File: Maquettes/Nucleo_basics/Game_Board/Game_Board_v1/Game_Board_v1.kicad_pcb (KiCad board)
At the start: 2 copper layers, 150 x 100 mm, 42 parts, among them CON1 MikroE-nRF-S-module, J1 TFT-RB1.8, J2 JOYSTICK, J3 AnalogIn, J4 AnalogChoice, SW1 SW_Push, SW2 SW_Push, SW3 SW_Push, SW4 SW_Push, U1 NUCLEO-L432KC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

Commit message: Update GameBoard
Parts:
- removed R14, R15: 220, Resistor_THT:R_Axial_DIN0207_L6.3mm_D2.5mm_P10.16mm_Horizontal
- removed R16, R17, R18: 1k, Resistor_THT:R_Axial_DIN0207_L6.3mm_D2.5mm_P10.16mm_Horizontal
- added J5: Conn_01x02, TerminalBlock_Phoenix:TerminalBlock_Phoenix_PT-1,5-2-5.0-H_1x02_P5.00mm_Horizontal, F.Cu at (179.5, 154.5)
- added J6: Conn_01x04, Connector_PinHeader_2.54mm:PinHeader_1x04_P2.54mm_Horizontal, F.Cu at (259.1, 151.0)
- R11, R12, R13: value 220 -> 1k
- R3: value 220 -> 1.2k
- R4: value 220 -> 12k
- R5: value 1.2k -> 12k
- R8, R9: value 12k -> 220
- RV1: value R_POT_TRIM -> R_10k
- SW1, SW2, SW3, SW4: footprint Resistor_THT:R_Axial_DIN0207_L6.3mm_D2.5mm_P5.08mm_Vertical -> LEnsE_devices:Switch
- moved D1 135.8 mm to (147.9, 159.5)
- moved D2 132.6 mm to (148.0, 156.0)
- moved C5 132.4 mm to (154.0, 148.0), turned to 180 degrees
- moved R6 119.8 mm to (138.9, 146.6)
- moved R3 100.7 mm to (145.4, 152.1), turned to 0 degrees
- moved R10 95.2 mm to (239.3, 71.0), turned to 0 degrees
- moved R9 90.0 mm to (239.3, 75.0), turned to 0 degrees
- moved R8 88.8 mm to (261.8, 70.9), turned to 0 degrees
- moved R12 84.7 mm to (205.8, 149.0)
- moved R7 84.6 mm to (261.8, 75.0), turned to 0 degrees
- moved R2 78.1 mm to (259.3, 83.5), turned to 0 degrees
- moved R1 75.2 mm to (263.8, 89.0), turned to 0 degrees
- moved R11 73.8 mm to (205.8, 145.5), turned to 0 degrees
- moved U2 53.6 mm to (140.2, 84.1), turned to 90 degrees
- moved R5 52.8 mm to (240.5, 108.5), turned to -90 degrees
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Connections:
- C1 pad 1: SW1 -> 3.3V
- C1 pad 2: GND -> SW1
- C2 pad 1: SW2 -> 3.3V
- C2 pad 2: GND -> SW2
- C3 pad 1: SW_JOY_OUT -> 3.3V
- C3 pad 2: GND -> SW3
- C4 pad 1: SW3 -> 3.3V
- C4 pad 2: GND -> SW4
- C5 pad 1: SW4 -> 3.3V
- C5 pad 2: GND -> JOYSW
- D1 pad 2: Net-(D1-A) -> AN_IN
- D2 pad 1: Net-(D1-A) -> AN_IN
- D5 pad 1: unconnected-(D5-K-Pad1) -> Net-(D5-K)
- R1 pad 1: Net-(R1-Pad1) -> SW1
- R10 pad 1: Net-(R10-Pad1) -> Net-(D6-K)
- R10 pad 2: SW3 -> GND
- R11 pad 1: Net-(R11-Pad1) -> 3.3V
- R11 pad 2: SW4 -> SCL
- R12 pad 1: Net-(D3-K) -> 3.3V
- R12 pad 2: GND -> SDA
- R13 pad 1: Net-(D4-K) -> 3.3V
- R13 pad 2: GND -> Net-(U3-~{RESET})
- R2 pad 1: Net-(R2-Pad1) -> SW2
- R3 pad 1: Net-(R1-Pad1) -> Net-(J3-Pin_2)
- R3 pad 2: SW1 -> AN_IN
- R4 pad 1: Net-(R2-Pad1) -> SW3
- R4 pad 2: SW2 -> GND
- R5 pad 1: Net-(J3-Pin_2) -> SW4
- R5 pad 2: Net-(D1-A) -> GND
- R7 pad 1: JOYSW -> Net-(D3-K)
- R7 pad 2: SW_JOY_OUT -> GND
- R8 pad 1: Net-(R10-Pad1) -> Net-(D4-K)
- R9 pad 1: Net-(R11-Pad1) -> Net-(D5-K)
- SW1 pad 2: Net-(R1-Pad1) -> SW1
- SW2 pad 2: Net-(R2-Pad1) -> SW2
- SW3 pad 2: Net-(R10-Pad1) -> SW3
- SW4 pad 2: Net-(R11-Pad1) -> SW4
- U1 pad CN3_5: SW_JOY_OUT -> JOYSW
- U1 pad CN3_7: unconnected-(U1A-PB7-PadCN3_7) -> SDA
- U1 pad CN3_8: LCD_DC -> SCL
- U1 pad CN3_9: unconnected-(U1A-PB1-PadCN3_9) -> LCD_DC
- U1 pad CN4_1: unconnected-(U1B-VIN-PadCN4_1) -> Vin
- U1 pad CN4_4: unconnected-(U1B-+5V-PadCN4_4) -> 5V
- U1 pad CN4_7: SCL -> unconnected-(U1B-PA6-PadCN4_7)
- U1 pad CN4_8: SDA -> unconnected-(U1B-PA5-PadCN4_8)
- U2 pad 1: nRF_INT -> (no net)
- U2 pad 10: (no net) -> EX_nRF_INT
- U2 pad 2: EXP_INT -> (no net)
- U2 pad 3: EX_nRF_INT -> (no net)
- U2 pad 8: (no net) -> nRF_INT
- U2 pad 9: (no net) -> EXP_INT
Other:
- outline, holes or cut-outs redrawn

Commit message: Update GameBoard
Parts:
- added J10: nRF_temp1, Connector_PinSocket_2.54mm:PinSocket_1x02_P2.54mm_Vertical, F.Cu at (241.0, 133.5)
- added J11: nRF_temp2, Connector_PinSocket_2.54mm:PinSocket_1x02_P2.54mm_Vertical, F.Cu at (138.2, 71.6)
- added J7: LCD_TEMp, Connector_PinSocket_2.54mm:PinSocket_1x03_P2.54mm_Vertical, F.Cu at (210.6, 134.4)
- added J8: SD_CS_t1, Connector_PinSocket_2.54mm:PinSocket_1x01_P2.54mm_Vertical, F.Cu at (171.0, 130.6)
- added J9: SD_CS_t1, Connector_PinSocket_2.54mm:PinSocket_1x01_P2.54mm_Vertical, F.Cu at (223.3, 134.6)
- R10, R7, R8, R9: value 220 -> 100
- R11, R12, R13: value 1k -> 680
- moved U2 45.2 mm to (183.8, 71.8), turned to 0 degrees
- moved CON1 23.2 mm to (144.2, 69.1)
- moved R9 22.9 mm to (262.2, 73.7)
- moved R10 22.8 mm to (262.1, 70.4)
- moved R4 19.2 mm to (253.5, 93.5), turned to 180 degrees
- moved C3 18.0 mm to (244.4, 83.5), turned to 180 degrees
- moved R5 17.4 mm to (253.5, 97.0), turned to 180 degrees
- moved R7 15.3 mm to (246.6, 73.7)
- moved R8 15.3 mm to (246.6, 70.5)
- moved R13 15.1 mm to (200.0, 76.8), turned to -90 degrees
- moved C4 13.8 mm to (250.5, 89.0), turned to 180 degrees
- moved SW1 13.0 mm to (265.0, 108.5), turned to 0 degrees
- moved SW2 13.0 mm to (277.5, 112.0), turned to 90 degrees
- moved D3 7.60 mm to (218.4, 70.1)
- moved D4 7.24 mm to (213.0, 69.9)
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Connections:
- U1 pad CN3_1: nRF_CS -> nRF_CS_t
- U1 pad CN3_12: LCD_RES -> LCD_RES_t
- U1 pad CN3_13: EX_nRF_INT -> LCD_CS_t
- U1 pad CN3_2: nRF_RS -> nRF_RS_t
- U1 pad CN3_5: JOYSW -> EX_nRF_INT
- U1 pad CN3_6: SD_CS -> SD_CS_t
- U1 pad CN3_9: LCD_DC -> LCD_DC_t
- U1 pad CN4_6: LCD_CS -> AN_OUT
- U1 pad CN4_9: AN_OUT -> JOYSW
- U2 pad 10: EX_nRF_INT -> (no net)
- U2 pad 11: (no net) -> EX_nRF_INT
- U2 pad 12: (no net) -> nRF_INT
- U2 pad 13: (no net) -> EXP_INT
- U2 pad 8: nRF_INT -> (no net)
- U2 pad 9: EXP_INT -> (no net)
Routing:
- net 3.3V: track 0.00 -> 440.7 mm, vias 0 -> 10
- net SDA: track 0.00 -> 151.6 mm, vias 0 -> 2
- net SCL: track 0.00 -> 150.1 mm, vias 0 -> 2
- net SCK: track 0.00 -> 135.5 mm, vias 0 -> 4
- net EX_nRF_INT: track 0.00 -> 132.1 mm
- net MOSI: track 0.00 -> 109.3 mm
- net MISO: track 0.00 -> 108.9 mm, vias 0 -> 4
- net JOYSW: track 0.00 -> 106.3 mm
- net JOYY: track 0.00 -> 87.2 mm
- net JOYX: track 0.00 -> 81.6 mm
- net SW4: track 0.00 -> 76.5 mm
- net SW2: track 0.00 -> 75.2 mm
- net AN_OUT: track 0.00 -> 68.7 mm
- net Net-(D6-K): track 0.00 -> 66.3 mm
- net SW1: track 0.00 -> 63.0 mm
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- added copper zone on B.Cu, net GND
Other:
- outline, holes or cut-outs redrawn
- board text added: "LEnsE 2024 Game Board"

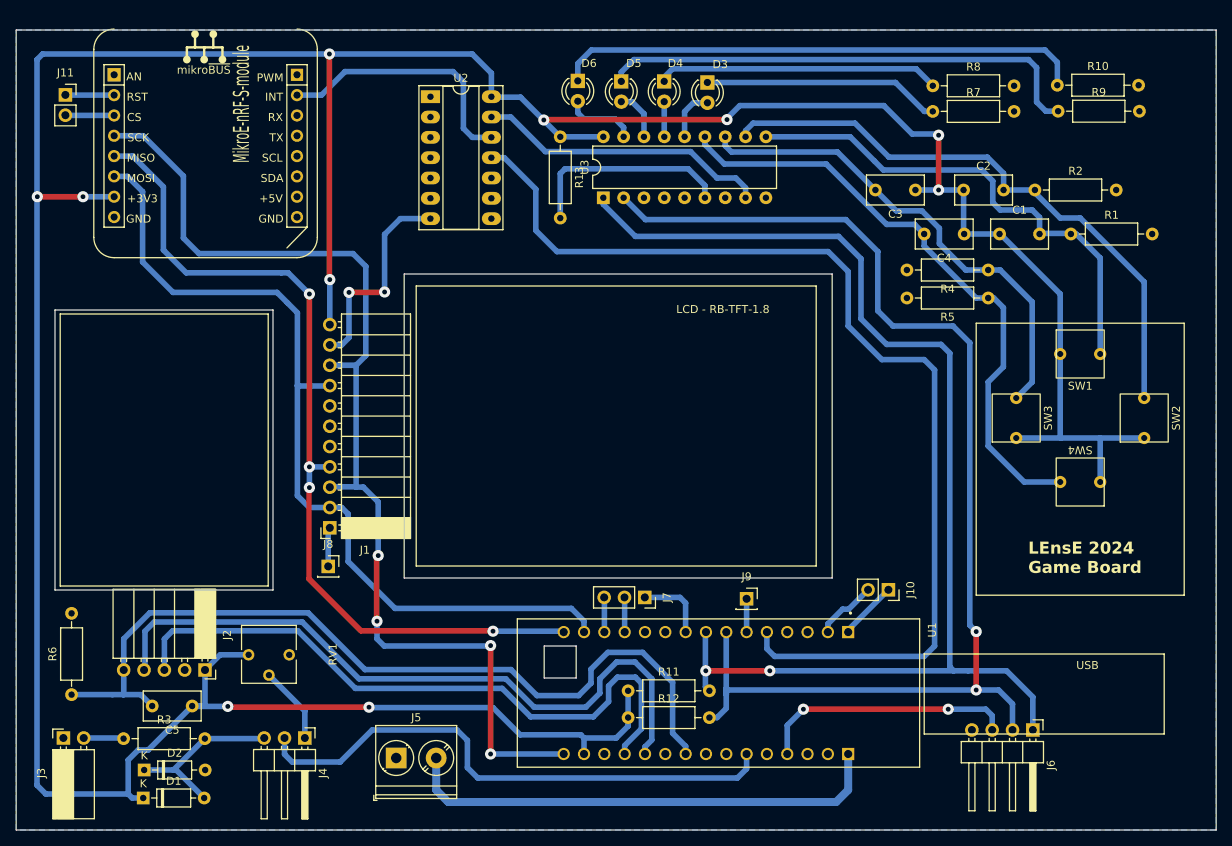
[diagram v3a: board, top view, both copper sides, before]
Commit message: Update Gameboard
Change Joystick connector !!
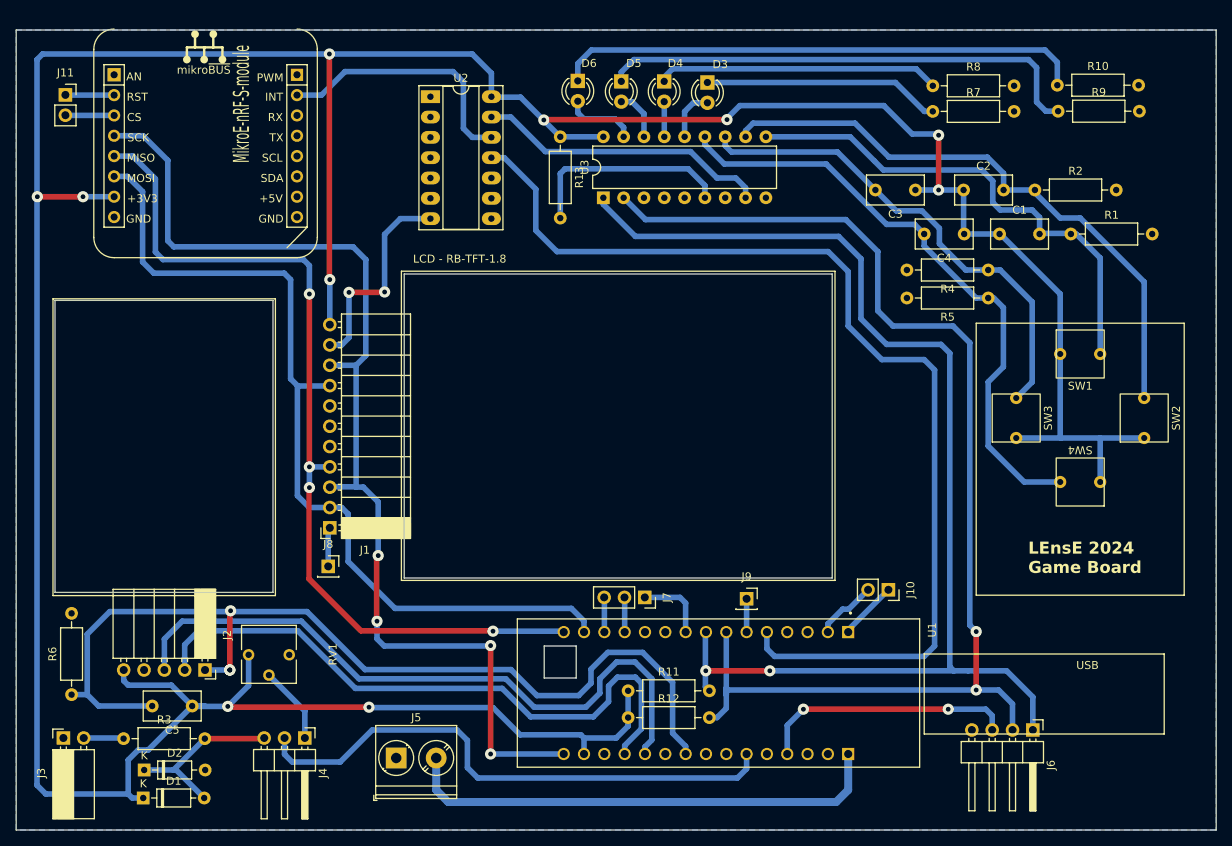
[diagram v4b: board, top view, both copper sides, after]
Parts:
- J6: value Conn_01x04 -> I2C_EXT
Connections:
- J2 pad 1: 3.3V -> JOYSW
- J2 pad 2: GND -> JOYY
- J2 pad 4: JOYY -> GND
- J2 pad 5: JOYSW -> 3.3V
- U1 pad CN4_11: JOYY -> JOYX
- U1 pad CN4_12: JOYX -> JOYY
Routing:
- net JOYSW: track 106.3 -> 121.9 mm, vias 0 -> 3
- net JOYY: track 87.2 -> 78.6 mm
- net 3.3V: track 440.7 -> 448.7 mm
- net MISO: track 108.9 -> 111.8 mm
- net JOYX: track 81.6 -> 84.2 mm
- net MOSI: track 109.3 -> 111.2 mm
- net SCK: track 135.5 -> 137.3 mm
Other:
- outline, holes or cut-outs redrawn

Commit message: Update GameBoard
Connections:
- net nRF_RS renamed nRF_CE
- net nRF_RS_t renamed nRF_CE_t
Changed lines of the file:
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@@
 	(net 11 "unconnected-(CON1-PWM-PadP16)")
 	(net 12 "nRF_INT")
-	(net 13 "nRF_RS")
+	(net 13 "nRF_CE")
 	(net 14 "MISO")
 	(net 15 "MOSI")
@@
 	(net 59 "SD_CS_t")
 	(net 60 "nRF_CS_t")
-	(net 61 "nRF_RS_t")
+	(net 61 "nRF_CE_t")
 	(footprint "Resistor_THT:R_Axial_DIN0207_L6.3mm_D2.5mm_P10.16mm_Horizontal"
 		(layer "F.Cu")
@@
 			(layers "*.Cu" "*.Mask")
 			(remove_unused_layers no)
-			(net 61 "nRF_RS_t")
+			(net 61 "nRF_CE_t")
 			(pinfunction "Pin_2")
 			(pintype "passive")
@@
 			(layers "*.Cu" "*.Mask")
 			(remove_unused_layers no)
-			(net 13 "nRF_RS")
+			(net 13 "nRF_CE")
 			(pinfunction "Pin_1")
 			(pintype "passive")
@@
 			(layers "*.Cu" "*.Mask")
 			(remove_unused_layers no)
-			(net 13 "nRF_RS")
+			(net 13 "nRF_CE")
 			(pinfunction "RST")
 			(pintype "bidirectional")
@@
 			(layers "*.Cu" "*.Mask")
 			(remove_unused_layers no)
-			(net 61 "nRF_RS_t")
+			(net 61 "nRF_CE_t")
 			(pinfunction "PA10")
 			(pintype "bidirectional")
